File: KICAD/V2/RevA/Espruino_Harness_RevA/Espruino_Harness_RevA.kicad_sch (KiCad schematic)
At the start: 4 parts, among them J2 Grove_I2C_1x04, J900 TARGET INTERFACE CONNECTOR A, J901 TARGET INTERFACE CONNECTOR B

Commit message: Integrate Rev-A rack control endpoint
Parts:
- added JBP2: Provisional BackPlane Connection, symbol Connector_Generic:Conn_02x06_Odd_Even
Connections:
- net TI_GND: now also JBP2.10 (Pin_10), JBP2.12 (Pin_12), JBP2.2 (Pin_2), JBP2.4 (Pin_4), JBP2.6 (Pin_6), JBP2.8 (Pin_8)
- new net RACK_INT_N: JBP2.1 (Pin_1)
- no-connect marks 0 -> 5
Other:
- added sheet V2 Rev-A Rack Control Endpoint (rack_control.kicad_sch)
- moved on the sheet: J900, J901

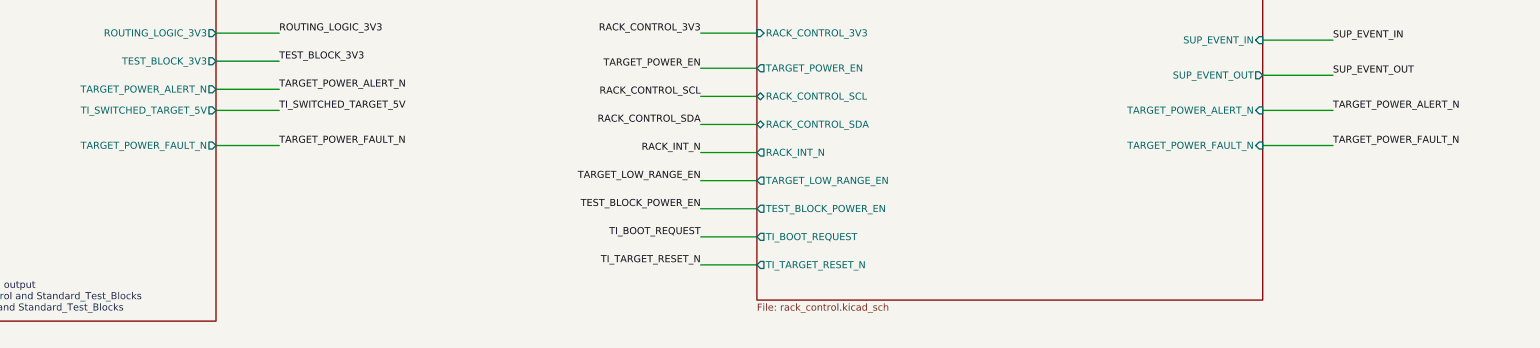
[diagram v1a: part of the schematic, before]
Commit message: Implement low-range power alert integration
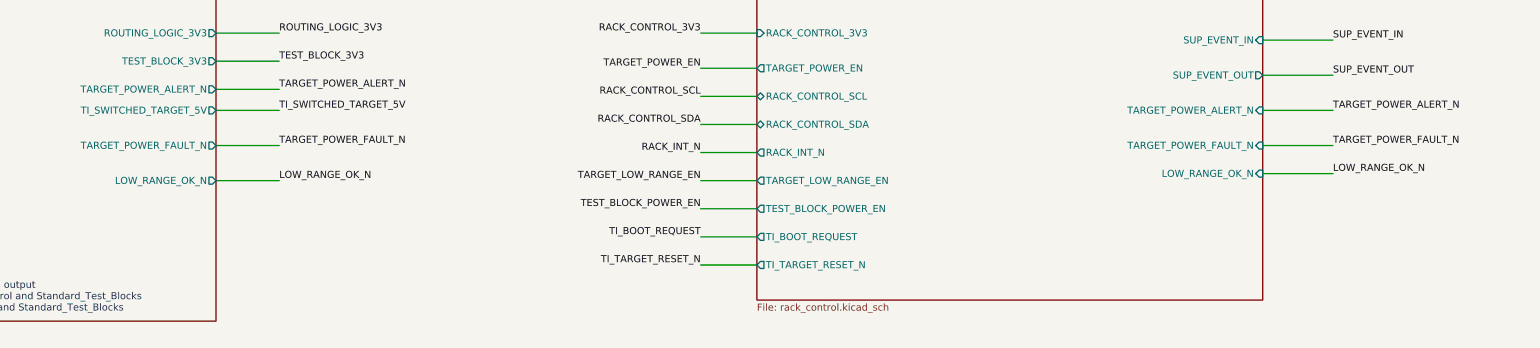
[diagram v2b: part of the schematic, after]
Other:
- sheet Power_Control ports: added LOW_RANGE_OK_N; removed none
- sheet V2 Rev-A Rack Control Endpoint ports: added LOW_RANGE_OK_N; removed none
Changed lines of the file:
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@@
 	(wire
 		(pts
+			(xy 325.12 91.44) (xy 337.82 91.44)
+		)
+		(stroke
+			(width 0)
+			(type default)
+		)
+	)
+	(wire
+		(pts
 			(xy 520.7 160.02) (xy 535.94 160.02)
 		)
@@
 	(wire
 		(pts
+			(xy 135.89 92.71) (xy 147.32 92.71)
+		)
+		(stroke
+			(width 0)
+			(type default)
+		)
+	)
+	(wire
+		(pts
 			(xy 43.18 267.97) (xy 55.88 267.97)
 		)
@@
 		)
 	)
+	(label "LOW_RANGE_OK_N"
+		(at 147.32 92.71 0)
+		(effects
+			(font
+				(size 1.27 1.27)
+			)
+			(justify left bottom)
+		)
+	)
 	(label "TI_GND"
 		(at 340.36 187.96 0)
@@
 		)
 	)
+	(label "LOW_RANGE_OK_N"
+		(at 337.82 91.44 0)
+		(effects
+			(font
+				(size 1.27 1.27)
+			)
+			(justify left bottom)
+		)
+	)
 	(label "TI_GPIO_LOOP_A_IN"
 		(at 535.94 58.42 0)
@@
 			)
 		)
+		(pin "LOW_RANGE_OK_N" output
+			(at 135.89 92.71 0)
+			(effects
+				(font
+					(size 1.27 1.27)
+				)
+				(justify right)
+			)
+		)
 		(instances
 			(project "Espruino_Harness_RevA"
@@
 			(effects
 				(font
+					(size 1.27 1.27)
+				)
+				(justify right)
+			)
+		)
+		(pin "LOW_RANGE_OK_N" input
+			(at 325.12 91.44 0)
+			(effects
+				(font

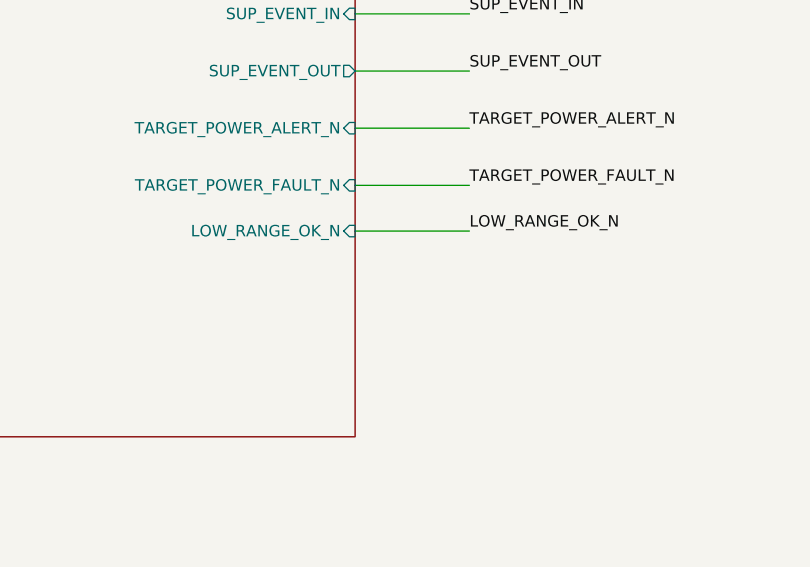
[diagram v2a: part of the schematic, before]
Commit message: Verify RC02 routing control baseline
Add the qualified fixed-I2C isolation and Hardware Clear implementation, exact component metadata, deterministic RC02 connectivity contract, accepted ERC/connectivity evidence, and visual review records. Synchronize the draft PCB and document the PCB-stage workflow while preserving the verified RC01 baseline.
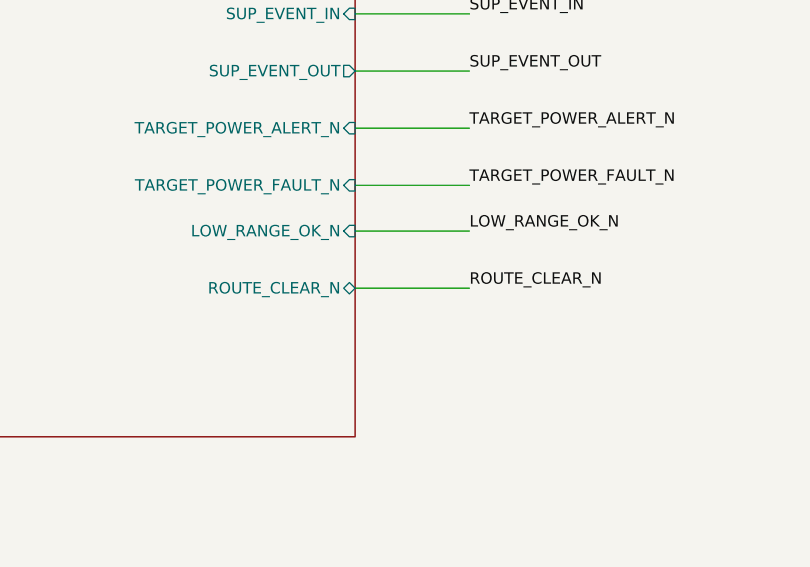
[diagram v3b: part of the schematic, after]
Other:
- sheet V2 Rev-A Rack Control Endpoint ports: added ROUTE_CLEAR_N; removed none
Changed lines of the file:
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@@
 	(wire
 		(pts
+			(xy 325.12 97.79) (xy 337.82 97.79)
+		)
+		(stroke
+			(width 0)
+			(type default)
+		)
+	)
+	(wire
+		(pts
 			(xy 36.83 85.09) (xy 43.18 85.09)
 		)
@@
 		)
 	)
+	(label "ROUTE_CLEAR_N"
+		(at 337.82 97.79 0)
+		(effects
+			(font
+				(size 1.27 1.27)
+			)
+			(justify left bottom)
+		)
+	)
 	(label "TI_TARGET_3V3"
 		(at 214.63 153.67 0)
@@
 			(effects
 				(font
+					(size 1.27 1.27)
+				)
+				(justify right)
+			)
+		)
+		(pin "ROUTE_CLEAR_N" bidirectional
+			(at 325.12 97.79 0)
+			(effects
+				(font

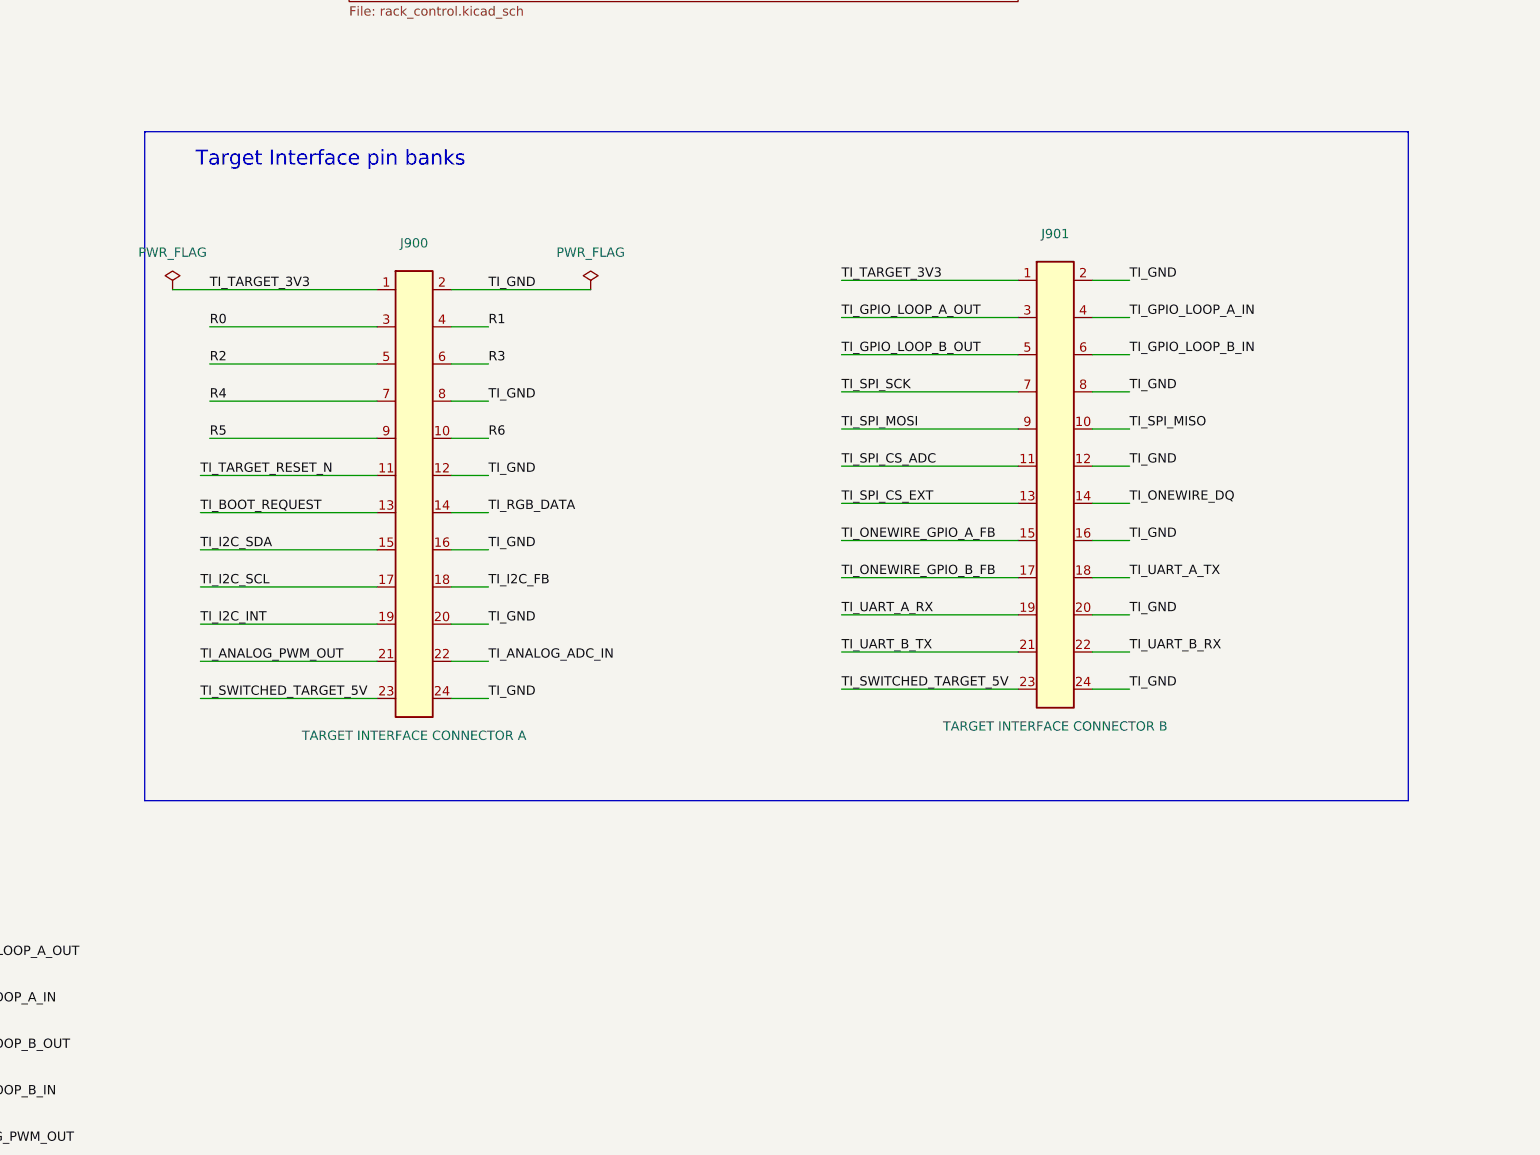
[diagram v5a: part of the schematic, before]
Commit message: Verify TI01 target interface baseline
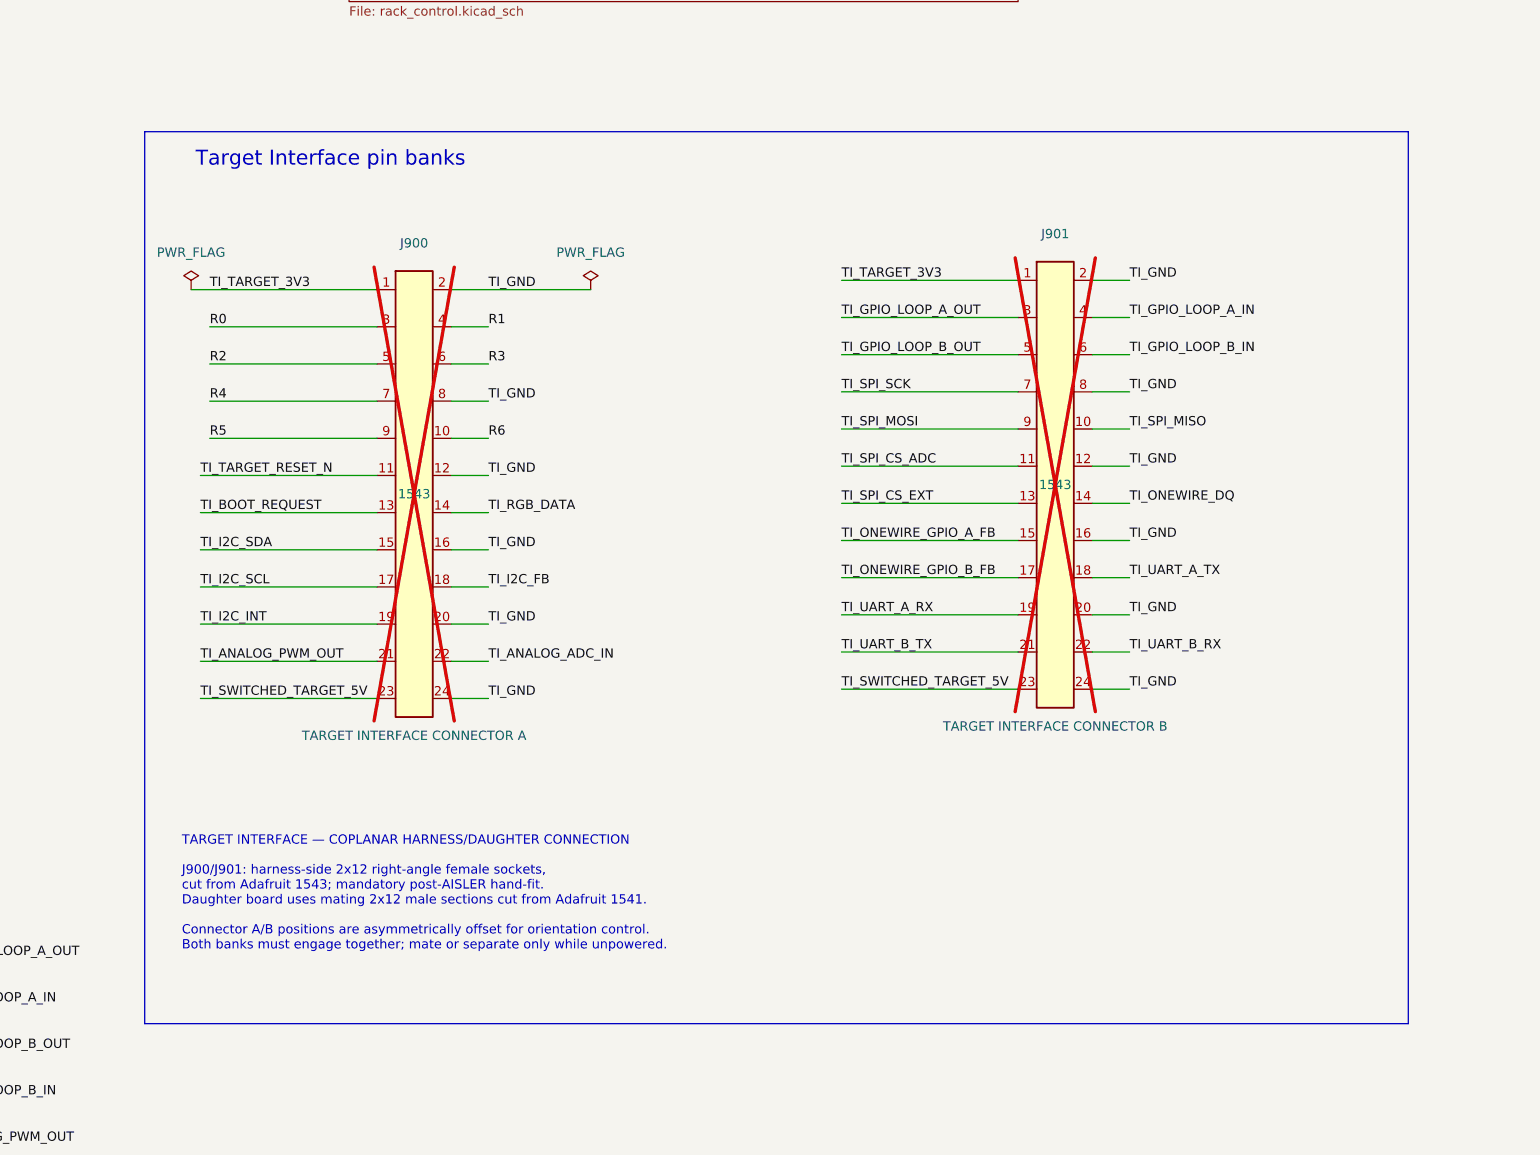
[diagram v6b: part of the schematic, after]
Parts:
- J900, J901: MPN (none) -> 1543; now not fitted
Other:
- note added: "TARGET INTERFACE — COPLANAR HARNESS/DAUGHTER CONNECTION J900/J901: harness-side 2x12 right-angle female sockets, cut from Adafruit 1543; mandatory post-AISLER hand-fit. Daughter board uses mating 2x12 male sections cut from Adafruit 1541. Connector A/B positions are asymmetrically offset for orientation control. Both banks must engage together; mate or separate only while unpowered."
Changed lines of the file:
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@@
 	(rectangle
 		(start 205.74 132.08)
-		(end 378.46 223.52)
+		(end 378.46 254)
 		(stroke
 			(width 0)
@@
 		)
 	)
+	(text "TARGET INTERFACE — COPLANAR HARNESS/DAUGHTER CONNECTION\n\nJ900/J901: harness-side 2x12 right-angle female sockets,\ncut from Adafruit 1543; mandatory post-AISLER hand-fit.\nDaughter board uses mating 2x12 male sections cut from Adafruit 1541.\n\nConnector A/B positions are asymmetrically offset for orientation control.\nBoth banks must engage together; mate or separate only while unpowered."
+		(exclude_from_sim no)
+		(at 210.82 236.22 0)
+		(effects
+			(font
+				(size 1.27 1.27)
+			)
+			(justify left)
+		)
+	)
 	(text "RACK POWER BACKPLANE INTERFACE - PROVISIONAL"
 		(exclude_from_sim no)
@@
 	(wire
 		(pts
-			(xy 209.55 153.67) (xy 237.49 153.67)
+			(xy 212.09 153.67) (xy 237.49 153.67)
 		)
 		(stroke
@@
 		(in_bom yes)
 		(on_board yes)
-		(dnp no)
+		(dnp yes)
 		(property "Reference" "J900"
 			(at 242.57 147.32 0)
@@
 			)
 		)
-		(property "Datasheet" "~"
+		(property "Datasheet" "https://cdn-shop.adafruit.com/datasheets/P1543.pdf"
 			(at 242.57 181.61 0)
 			(effects
@@
 			)
 		)
-		(property "Description" "V2 Target Interface connector bank; 2x12 odd/even contact numbering"
+		(property "Description" "Target Interface A harness socket; 2x12 cut from Adafruit 1543; post-AISLER hand-fit"
 			(at 242.57 181.61 0)
 			(effects
@@
 			)
 		)
-		(property "DNP" ""
+		(property "MPN" "1543"
+			(at 242.57 181.61 0)
+			(effects
+				(font
+					(size 1.27 1.27)
+				)
+			)
+		)
+		(property "AISLER_MPN" ""
 			(at 242.57 181.61 0)
 			(effects
@@
 					(size 1.27 1.27)
 				)
-				(hide yes)
 			)
 		)
@@
 	(symbol
 		(lib_id "power:PWR_FLAG")
-		(at 209.55 153.67 0)
+		(at 212.09 153.67 0)
 		(unit 1)
 		(exclude_from_sim no)
@@
 		(fields_autoplaced yes)
 		(property "Reference" "#FLG03"
-			(at 209.55 151.765 0)
+			(at 212.09 151.765 0)
 			(effects
 				(font
@@
 		)
 		(property "Value" "PWR_FLAG"
-			(at 209.55 148.59 0)
+			(at 212.09 148.59 0)
 			(effects
 				(font
@@
 		)
 		(property "Footprint" ""
-			(at 209.55 153.67 0)
+			(at 212.09 153.67 0)
 			(effects
 				(font
@@
 		)
 		(property "Datasheet" "~"
-			(at 209.55 153.67 0)
+			(at 212.09 153.67 0)
 			(effects
 				(font
@@
 		)
 		(property "Description" "Special symbol for telling ERC where power comes from"
-			(at 209.55 153.67 0)
+			(at 212.09 153.67 0)
 			(effects
 				(font
@@
 		(in_bom yes)
 		(on_board yes)
-		(dnp no)
+		(dnp yes)
 		(property "Reference" "J901"
 			(at 330.2 146.05 0)
@@
 			)
 		)
-		(property "Datasheet" "~"
+		(property "Datasheet" "https://cdn-shop.adafruit.com/datasheets/P1543.pdf"
 			(at 330.2 180.34 0)
 			(effects
@@
 			)
 		)
-		(property "Description" "V2 Target Interface connector bank; 2x12 odd/even contact numbering"
+		(property "Description" "Target Interface B harness socket; 2x12 cut from Adafruit 1543; post-AISLER hand-fit"
 			(at 330.2 180.34 0)
 			(effects
@@
 			)
 		)
-		(property "DNP" ""
+		(property "MPN" "1543"
+			(at 330.2 180.34 0)
+			(effects
+				(font
+					(size 1.27 1.27)
+				)
+			)
+		)
+		(property "AISLER_MPN" ""
 			(at 330.2 180.34 0)
 			(effects
@@
 					(size 1.27 1.27)
 				)
-				(hide yes)
 			)
 		)

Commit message: Implement Rev-A daughter-board foundations
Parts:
- J900, J901: footprint (none) -> V2_Target_Interface:TargetInterface_2x12_P2.54mm_RA_Female_Adafruit1543_Harness
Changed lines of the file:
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@@
 			)
 		)
-		(property "Footprint" ""
+		(property "Footprint" "V2_Target_Interface:TargetInterface_2x12_P2.54mm_RA_Female_Adafruit1543_Harness"
 			(at 242.57 181.61 0)
 			(effects
@@
 			)
 		)
-		(property "Footprint" ""
+		(property "Footprint" "V2_Target_Interface:TargetInterface_2x12_P2.54mm_RA_Female_Adafruit1543_Harness"
 			(at 330.2 180.34 0)
 			(effects

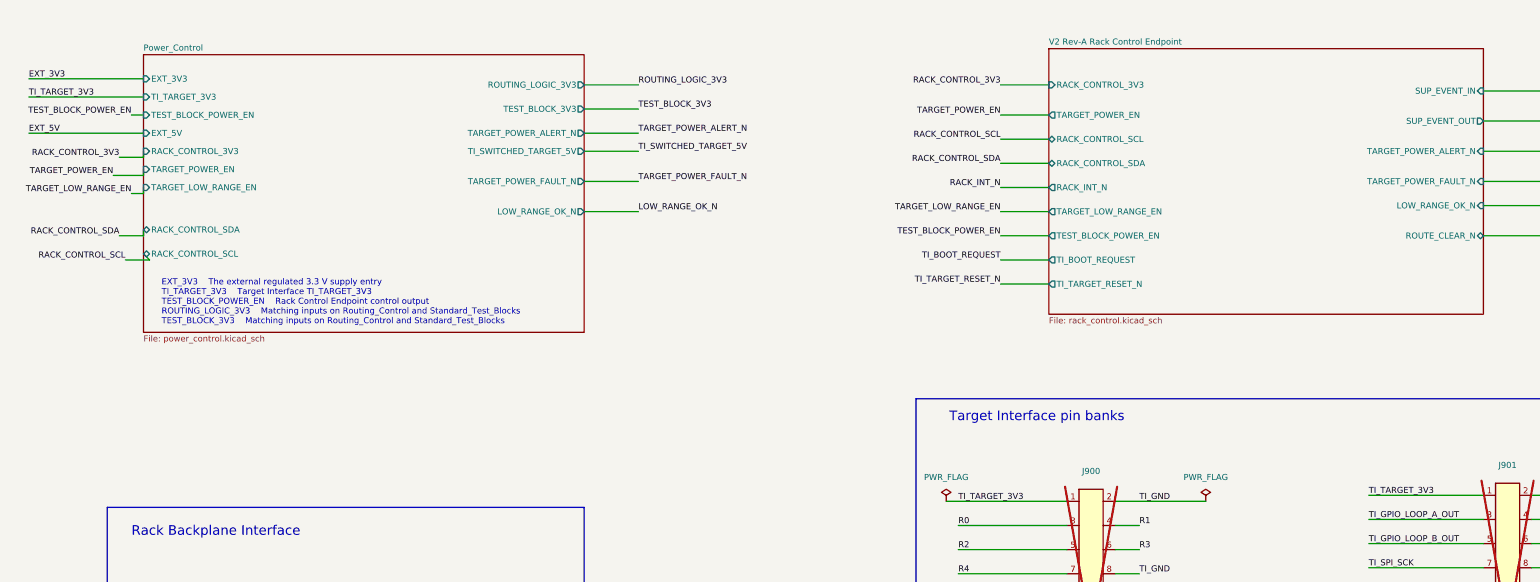
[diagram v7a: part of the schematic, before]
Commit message: Correct Rev-A operating-mode power architecture
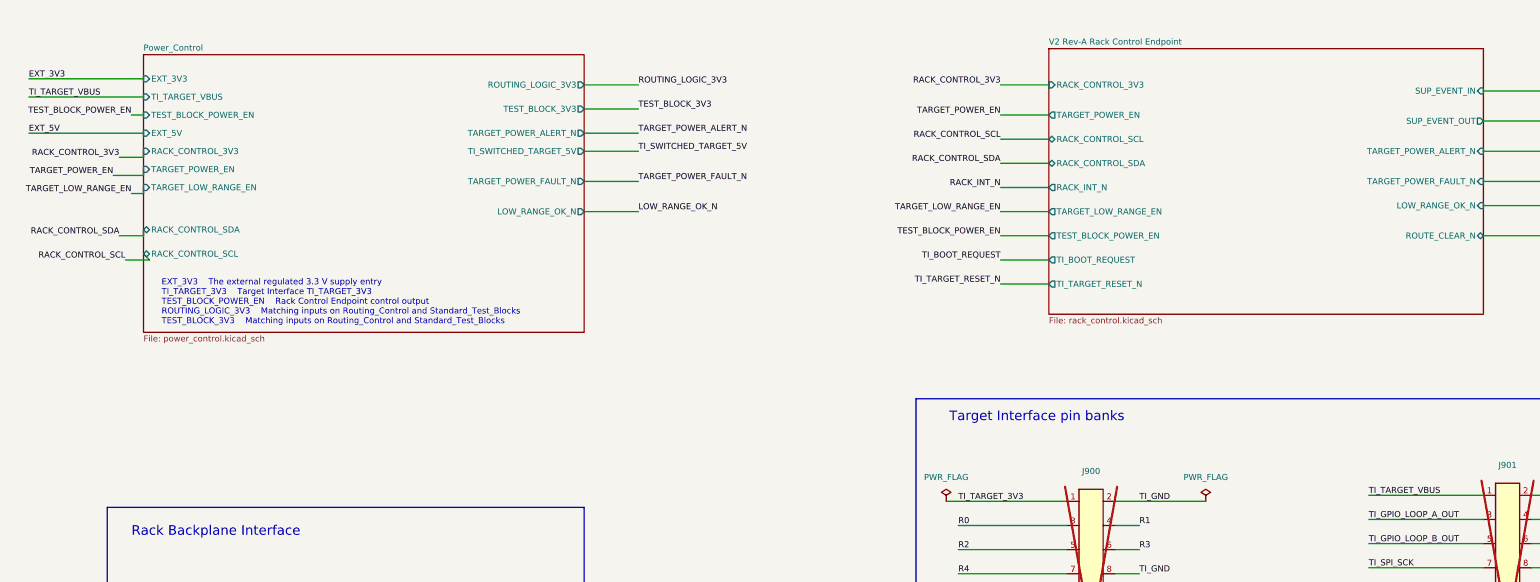
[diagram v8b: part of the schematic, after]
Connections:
- net TI_TARGET_3V3: no longer J901.1 (Contact_01)
- new net TI_TARGET_VBUS: J901.1 (Contact_01)
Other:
- sheet Power_Control ports: added TI_TARGET_VBUS; removed TI_TARGET_3V3
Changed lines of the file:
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@@
 		)
 	)
-	(label "TI_TARGET_3V3"
+	(label "TI_TARGET_VBUS"
 		(at 300.99 152.4 0)
 		(effects
@@
 		)
 	)
-	(label "TI_TARGET_3V3"
+	(label "TI_TARGET_VBUS"
 		(at 19.05 68.58 0)
 		(effects
@@
 			)
 		)
-		(pin "TI_TARGET_3V3" input
+		(pin "TI_TARGET_VBUS" input
 			(at 43.18 68.58 180)
 			(effects
